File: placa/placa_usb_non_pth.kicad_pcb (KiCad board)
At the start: 2 copper layers, 84.6 x 25.4 mm, 23 parts, among them P5 USB_A, P6 ISP, P7 Targ., U1 74HC125N, U2 ATTINY2313DIP/SO, X1 12MHz

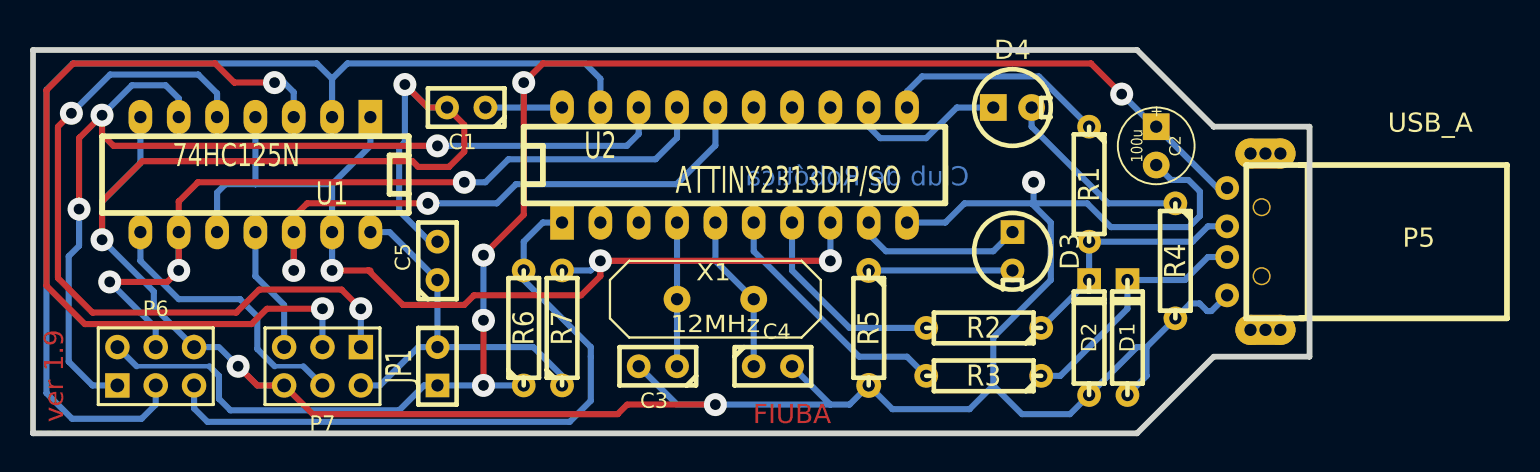
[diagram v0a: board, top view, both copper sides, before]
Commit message: arregle la serigrafia y corregi algunos detalles, mande a fabricar una
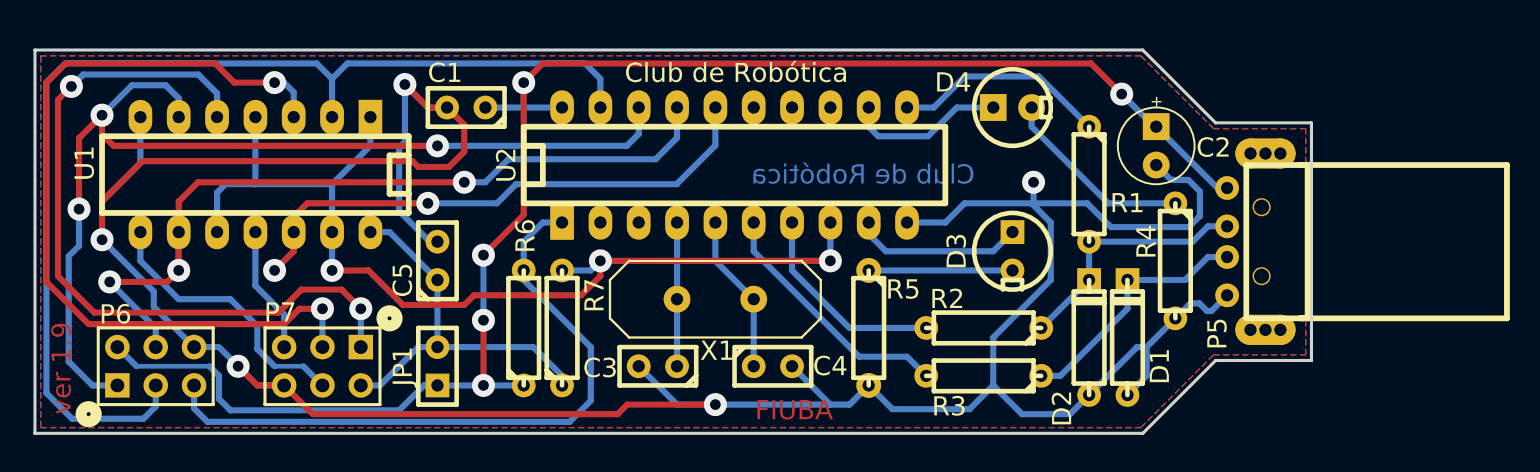
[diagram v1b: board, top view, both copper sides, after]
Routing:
- net /RST_B: track 38.5 -> 39.6 mm
- net N-0000029: track 48.3 -> 49.3 mm
- net /PD6: track 14.9 -> 14.3 mm
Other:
- outline, holes or cut-outs redrawn
